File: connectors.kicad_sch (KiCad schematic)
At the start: 4 parts

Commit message: test changes
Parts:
- gave numbers to parts that had none: 4
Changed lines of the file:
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@@
   (symbol (lib_id "Connector:Conn_01x04_Male") (at 83.82 48.006 0) (unit 1)
     (in_bom yes) (on_board yes)
-    (property "Reference" "J?" (id 0) (at 84.455 40.64 0))
+    (property "Reference" "J2" (id 0) (at 84.455 40.64 0))
     (property "Value" "Conn_01x04_Male" (id 1) (at 84.455 43.18 0))
     (property "Footprint" "" (id 2) (at 83.82 48.006 0)
@@
   (symbol (lib_id "Connector:Conn_01x04_Male") (at 64.77 48.006 0) (unit 1)
     (in_bom yes) (on_board yes)
-    (property "Reference" "J?" (id 0) (at 65.405 40.64 0))
+    (property "Reference" "J1" (id 0) (at 65.405 40.64 0))
     (property "Value" "Conn_01x04_Male" (id 1) (at 65.405 43.18 0))
     (property "Footprint" "" (id 2) (at 64.77 48.006 0)
@@
   (symbol (lib_id "Connector_Generic:Conn_02x03_Odd_Even") (at 93.218 83.566 0) (unit 1)
     (in_bom yes) (on_board yes)
-    (property "Reference" "J?" (id 0) (at 94.488 74.93 0))
+    (property "Reference" "J3" (id 0) (at 94.488 74.93 0))
     (property "Value" "Conn_02x03_Odd_Even" (id 1) (at 94.488 77.47 0))
     (property "Footprint" "" (id 2) (at 93.218 83.566 0)
@@
   (symbol (lib_id "Connector:Conn_01x09_Male") (at 64.516 84.074 0) (unit 1)
     (in_bom yes) (on_board yes)
-    (property "Reference" "J?" (id 0) (at 65.151 69.088 0))
+    (property "Reference" "J4" (id 0) (at 65.151 69.088 0))
     (property "Value" "Conn_01x09_Male" (id 1) (at 65.151 71.628 0))
     (property "Footprint" "" (id 2) (at 64.516 84.074 0)

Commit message: added the symbols anb the footprints to every component
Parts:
- J1, J2: footprint (none) -> Connector_PinHeader_2.54mm:PinHeader_1x04_P2.54mm_Vertical
- J3: footprint (none) -> Connector_PinHeader_2.54mm:PinHeader_2x03_P2.54mm_Vertical
- J4: footprint (none) -> Connector_PinHeader_2.54mm:PinHeader_1x09_P2.54mm_Vertical
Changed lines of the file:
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@@
     (property "Reference" "J2" (id 0) (at 84.455 40.64 0))
     (property "Value" "Conn_01x04_Male" (id 1) (at 84.455 43.18 0))
-    (property "Footprint" "" (id 2) (at 83.82 48.006 0)
+    (property "Footprint" "Connector_PinHeader_2.54mm:PinHeader_1x04_P2.54mm_Vertical" (id 2) (at 83.82 48.006 0)
       (effects (font (size 1.27 1.27)) hide)
     )
@@
     (property "Reference" "J1" (id 0) (at 65.405 40.64 0))
     (property "Value" "Conn_01x04_Male" (id 1) (at 65.405 43.18 0))
-    (property "Footprint" "" (id 2) (at 64.77 48.006 0)
+    (property "Footprint" "Connector_PinHeader_2.54mm:PinHeader_1x04_P2.54mm_Vertical" (id 2) (at 64.77 48.006 0)
       (effects (font (size 1.27 1.27)) hide)
     )
@@
     (property "Reference" "J3" (id 0) (at 94.488 74.93 0))
     (property "Value" "Conn_02x03_Odd_Even" (id 1) (at 94.488 77.47 0))
-    (property "Footprint" "" (id 2) (at 93.218 83.566 0)
+    (property "Footprint" "Connector_PinHeader_2.54mm:PinHeader_2x03_P2.54mm_Vertical" (id 2) (at 93.218 83.566 0)
       (effects (font (size 1.27 1.27)) hide)
     )
@@
     (property "Reference" "J4" (id 0) (at 65.151 69.088 0))
     (property "Value" "Conn_01x09_Male" (id 1) (at 65.151 71.628 0))
-    (property "Footprint" "" (id 2) (at 64.516 84.074 0)
+    (property "Footprint" "Connector_PinHeader_2.54mm:PinHeader_1x09_P2.54mm_Vertical" (id 2) (at 64.516 84.074 0)
       (effects (font (size 1.27 1.27)) hide)
     )

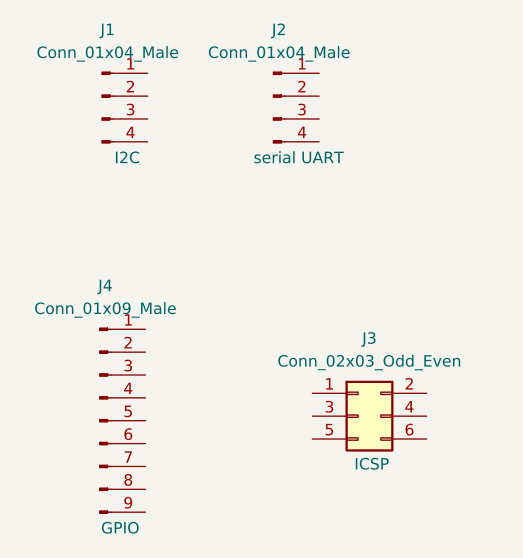
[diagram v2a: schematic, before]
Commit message: modificaciones en los nombres de los conectores
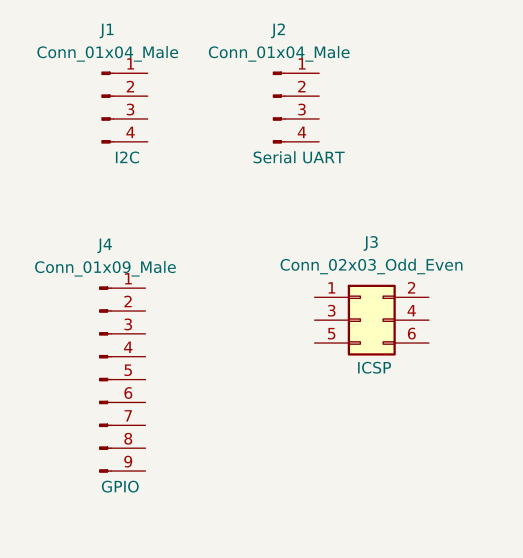
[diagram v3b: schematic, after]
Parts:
- J2: purpose serial UART -> Serial UART
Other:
- moved on the sheet: J3, J4
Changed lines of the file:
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@@
       (effects (font (size 1.27 1.27)) hide)
     )
-    (property "purpose" "serial UART" (id 4) (at 86.614 54.864 0))
+    (property "purpose" "Serial UART" (id 4) (at 86.614 54.864 0))
     (pin "1")
     (pin "2")
@@
     (pin "4")
   )
-  (symbol (lib_id "Connector_Generic:Conn_02x03_Odd_Even") (at 93.218 83.566 0) (unit 1)
+  (symbol (lib_id "Connector_Generic:Conn_02x03_Odd_Even") (at 93.472 72.898 0) (unit 1)
     (in_bom yes) (on_board yes)
-    (property "Reference" "J3" (id 0) (at 94.488 74.93 0))
-    (property "Value" "Conn_02x03_Odd_Even" (id 1) (at 94.488 77.47 0))
-    (property "Footprint" "Connector_PinHeader_2.54mm:PinHeader_2x03_P2.54mm_Vertical" (id 2) (at 93.218 83.566 0)
+    (property "Reference" "J3" (id 0) (at 94.742 64.262 0))
+    (property "Value" "Conn_02x03_Odd_Even" (id 1) (at 94.742 66.802 0))
+    (property "Footprint" "Connector_PinHeader_2.54mm:PinHeader_2x03_P2.54mm_Vertical" (id 2) (at 93.472 72.898 0)
       (effects (font (size 1.27 1.27)) hide)
     )
-    (property "Datasheet" "~" (id 3) (at 93.218 83.566 0)
+    (property "Datasheet" "~" (id 3) (at 93.472 72.898 0)
       (effects (font (size 1.27 1.27)) hide)
     )
-    (property "purpose" "ICSP" (id 4) (at 94.742 88.9 0))
+    (property "purpose" "ICSP" (id 4) (at 94.996 78.232 0))
     (pin "1")
     (pin "2")
@@
     (pin "6")
   )
-  (symbol (lib_id "Connector:Conn_01x09_Male") (at 64.516 84.074 0) (unit 1)
+  (symbol (lib_id "Connector:Conn_01x09_Male") (at 64.516 79.502 0) (unit 1)
     (in_bom yes) (on_board yes)
-    (property "Reference" "J4" (id 0) (at 65.151 69.088 0))
-    (property "Value" "Conn_01x09_Male" (id 1) (at 65.151 71.628 0))
-    (property "Footprint" "Connector_PinHeader_2.54mm:PinHeader_1x09_P2.54mm_Vertical" (id 2) (at 64.516 84.074 0)
+    (property "Reference" "J4" (id 0) (at 65.151 64.516 0))
+    (property "Value" "Conn_01x09_Male" (id 1) (at 65.151 67.056 0))
+    (property "Footprint" "Connector_PinHeader_2.54mm:PinHeader_1x09_P2.54mm_Vertical" (id 2) (at 64.516 79.502 0)
       (effects (font (size 1.27 1.27)) hide)
     )
-    (property "Datasheet" "~" (id 3) (at 64.516 84.074 0)
+    (property "Datasheet" "~" (id 3) (at 64.516 79.502 0)
       (effects (font (size 1.27 1.27)) hide)
     )
-    (property "purpose" "GPIO" (id 4) (at 66.802 96.012 0))
+    (property "purpose" "GPIO" (id 4) (at 66.802 91.44 0))
     (pin "1")
     (pin "2")

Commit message: cableado c asi terminado, dos error aun
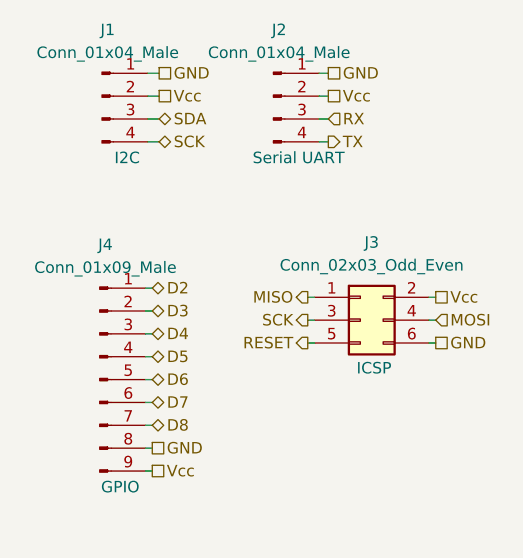
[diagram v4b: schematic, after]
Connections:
- net GND: now reaches J2.1 (Pin_1)
- net GND: now also J1.1 (Pin_1), J3.6 (Pin_6), J4.8 (Pin_8)
- net Vcc: now reaches J2.2 (Pin_2)
- net Vcc: now also J1.2 (Pin_2), J3.2 (Pin_2), J4.9 (Pin_9)
- net RX: now reaches J2.3 (Pin_3)
- net TX: now reaches J2.4 (Pin_4)
- net SDA: now reaches J1.3 (Pin_3)
- net SCK: now reaches J1.4 (Pin_4)
- net SCK: now also J3.3 (Pin_3)
- net MISO: now reaches J3.1 (Pin_1)
- net MOSI: now reaches J3.4 (Pin_4)
- net RESET: now reaches J3.5 (Pin_5)
- net D2: now reaches J4.1 (Pin_1)
- net D3: now reaches J4.2 (Pin_2)
- net D4: now reaches J4.3 (Pin_3)
- net D5: now reaches J4.4 (Pin_4)
- net D6: now reaches J4.5 (Pin_5)
- net D7: now reaches J4.6 (Pin_6)
- net D8: now reaches J4.7 (Pin_7)
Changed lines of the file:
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@@
 (kicad_sch (version 20211123) (generator eeschema)
   (paper "A4")
+  (wire (pts (xy 70.358 76.962) (xy 69.596 76.962))
+    (stroke (width 0) (type default) (color 0 0 0 0))
+  )
+  (wire (pts (xy 87.63 75.438) (xy 88.392 75.438))
+    (stroke (width 0) (type default) (color 0 0 0 0))
+  )
+  (wire (pts (xy 87.63 70.358) (xy 88.392 70.358))
+    (stroke (width 0) (type default) (color 0 0 0 0))
+  )
+  (wire (pts (xy 70.358 89.662) (xy 69.596 89.662))
+    (stroke (width 0) (type default) (color 0 0 0 0))
+  )
+  (wire (pts (xy 70.358 69.342) (xy 69.596 69.342))
+    (stroke (width 0) (type default) (color 0 0 0 0))
+  )
+  (wire (pts (xy 70.358 71.882) (xy 69.596 71.882))
+    (stroke (width 0) (type default) (color 0 0 0 0))
+  )
+  (wire (pts (xy 87.63 72.898) (xy 88.392 72.898))
+    (stroke (width 0) (type default) (color 0 0 0 0))
+  )
+  (wire (pts (xy 71.12 45.466) (xy 69.85 45.466))
+    (stroke (width 0) (type default) (color 0 0 0 0))
+  )
+  (wire (pts (xy 89.916 50.546) (xy 88.9 50.546))
+    (stroke (width 0) (type default) (color 0 0 0 0))
+  )
+  (wire (pts (xy 70.358 82.042) (xy 69.596 82.042))
+    (stroke (width 0) (type default) (color 0 0 0 0))
+  )
+  (wire (pts (xy 71.12 53.086) (xy 69.85 53.086))
+    (stroke (width 0) (type default) (color 0 0 0 0))
+  )
+  (wire (pts (xy 70.358 74.422) (xy 69.596 74.422))
+    (stroke (width 0) (type default) (color 0 0 0 0))
+  )
+  (wire (pts (xy 70.358 79.502) (xy 69.596 79.502))
+    (stroke (width 0) (type default) (color 0 0 0 0))
+  )
+  (wire (pts (xy 101.854 70.358) (xy 101.092 70.358))
+    (stroke (width 0) (type default) (color 0 0 0 0))
+  )
+  (wire (pts (xy 70.358 84.582) (xy 69.596 84.582))
+    (stroke (width 0) (type default) (color 0 0 0 0))
+  )
+  (wire (pts (xy 101.854 75.438) (xy 101.092 75.438))
+    (stroke (width 0) (type default) (color 0 0 0 0))
+  )
+  (wire (pts (xy 101.854 72.898) (xy 101.092 72.898))
+    (stroke (width 0) (type default) (color 0 0 0 0))
+  )
+  (wire (pts (xy 89.916 48.006) (xy 88.9 48.006))
+    (stroke (width 0) (type default) (color 0 0 0 0))
+  )
+  (wire (pts (xy 71.12 48.006) (xy 69.85 48.006))
+    (stroke (width 0) (type default) (color 0 0 0 0))
+  )
+  (wire (pts (xy 71.12 50.546) (xy 69.85 50.546))
+    (stroke (width 0) (type default) (color 0 0 0 0))
+  )
+  (wire (pts (xy 89.916 53.086) (xy 88.9 53.086))
+    (stroke (width 0) (type default) (color 0 0 0 0))
+  )
+  (wire (pts (xy 70.358 87.122) (xy 69.596 87.122))
+    (stroke (width 0) (type default) (color 0 0 0 0))
+  )
+  (wire (pts (xy 89.916 45.466) (xy 88.9 45.466))
+    (stroke (width 0) (type default) (color 0 0 0 0))
+  )
+  (hierarchical_label "D5" (shape bidirectional) (at 70.358 76.962 0)
+    (effects (font (size 1.27 1.27)) (justify left))
+  )
+  (hierarchical_label "GND" (shape passive) (at 70.358 87.122 0)
+    (effects (font (size 1.27 1.27)) (justify left))
+  )
+  (hierarchical_label "GND" (shape passive) (at 71.12 45.466 0)
+    (effects (font (size 1.27 1.27)) (justify left))
+  )
+  (hierarchical_label "D4" (shape bidirectional) (at 70.358 74.422 0)
+    (effects (font (size 1.27 1.27)) (justify left))
+  )
+  (hierarchical_label "SCK" (shape output) (at 87.63 72.898 180)
+    (effects (font (size 1.27 1.27)) (justify right))
+  )
+  (hierarchical_label "D6" (shape bidirectional) (at 70.358 79.502 0)
+    (effects (font (size 1.27 1.27)) (justify left))
+  )
+  (hierarchical_label "GND" (shape passive) (at 89.916 45.466 0)
+    (effects (font (size 1.27 1.27)) (justify left))
+  )
+  (hierarchical_label "MISO" (shape output) (at 87.63 70.358 180)
+    (effects (font (size 1.27 1.27)) (justify right))
+  )
+  (hierarchical_label "RESET" (shape output) (at 87.63 75.438 180)
+    (effects (font (size 1.27 1.27)) (justify right))
+  )
+  (hierarchical_label "D8" (shape bidirectional) (at 70.358 84.582 0)
+    (effects (font (size 1.27 1.27)) (justify left))
+  )
+  (hierarchical_label "Vcc" (shape passive) (at 101.854 70.358 0)
+    (effects (font (size 1.27 1.27)) (justify left))
+  )
+  (hierarchical_label "Vcc" (shape passive) (at 71.12 48.006 0)
+    (effects (font (size 1.27 1.27)) (justify left))
+  )
+  (hierarchical_label "TX" (shape output) (at 89.916 53.086 0)
+    (effects (font (size 1.27 1.27)) (justify left))
+  )
+  (hierarchical_label "Vcc" (shape passive) (at 70.358 89.662 0)
+    (effects (font (size 1.27 1.27)) (justify left))
+  )
+  (hierarchical_label "D3" (shape bidirectional) (at 70.358 71.882 0)
+    (effects (font (size 1.27 1.27)) (justify left))
+  )
+  (hierarchical_label "D2" (shape bidirectional) (at 70.358 69.342 0)
+    (effects (font (size 1.27 1.27)) (justify left))
+  )
+  (hierarchical_label "D7" (shape bidirectional) (at 70.358 82.042 0)
+    (effects (font (size 1.27 1.27)) (justify left))
+  )
+  (hierarchical_label "RX" (shape input) (at 89.916 50.546 0)
+    (effects (font (size 1.27 1.27)) (justify left))
+  )
+  (hierarchical_label "GND" (shape passive) (at 101.854 75.438 0)
+    (effects (font (size 1.27 1.27)) (justify left))
+  )
+  (hierarchical_label "SDA" (shape bidirectional) (at 71.12 50.546 0)
+    (effects (font (size 1.27 1.27)) (justify left))
+  )
+  (hierarchical_label "Vcc" (shape passive) (at 89.916 48.006 0)
+    (effects (font (size 1.27 1.27)) (justify left))
+  )
+  (hierarchical_label "MOSI" (shape input) (at 101.854 72.898 0)
+    (effects (font (size 1.27 1.27)) (justify left))
+  )
+  (hierarchical_label "SCK" (shape bidirectional) (at 71.12 53.086 0)
+    (effects (font (size 1.27 1.27)) (justify left))
+  )
   (symbol (lib_id "Connector:Conn_01x04_Male") (at 83.82 48.006 0) (unit 1)
     (in_bom yes) (on_board yes)

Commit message: cambio de nombre a las etiquetas, de Vcc a VCC, para que todas las etiquetas tengan el mismo nombre
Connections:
- net Vcc renamed VCC
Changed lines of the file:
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@@
     (effects (font (size 1.27 1.27)) (justify left))
   )
-  (hierarchical_label "Vcc" (shape passive) (at 101.854 70.358 0)
+  (hierarchical_label "VCC" (shape passive) (at 101.854 70.358 0)
     (effects (font (size 1.27 1.27)) (justify left))
   )
-  (hierarchical_label "Vcc" (shape passive) (at 71.12 48.006 0)
+  (hierarchical_label "VCC" (shape passive) (at 71.12 48.006 0)
     (effects (font (size 1.27 1.27)) (justify left))
   )
@@
     (effects (font (size 1.27 1.27)) (justify left))
   )
-  (hierarchical_label "Vcc" (shape passive) (at 70.358 89.662 0)
+  (hierarchical_label "VCC" (shape passive) (at 70.358 89.662 0)
     (effects (font (size 1.27 1.27)) (justify left))
   )
@@
     (effects (font (size 1.27 1.27)) (justify left))
   )
-  (hierarchical_label "Vcc" (shape passive) (at 89.916 48.006 0)
+  (hierarchical_label "VCC" (shape passive) (at 89.916 48.006 0)
     (effects (font (size 1.27 1.27)) (justify left))
   )
